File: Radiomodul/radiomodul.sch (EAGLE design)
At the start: 39 parts, among them IC1 ATMEGA2561-16AI, IC2 MCP42050, IC3 E910.15, IC4 AVR-JTAG, IC5 MAX232ECWE, IC6 MCP601SN, IC7 TLE42754D, J1 39-30-1100, Q1 16000000

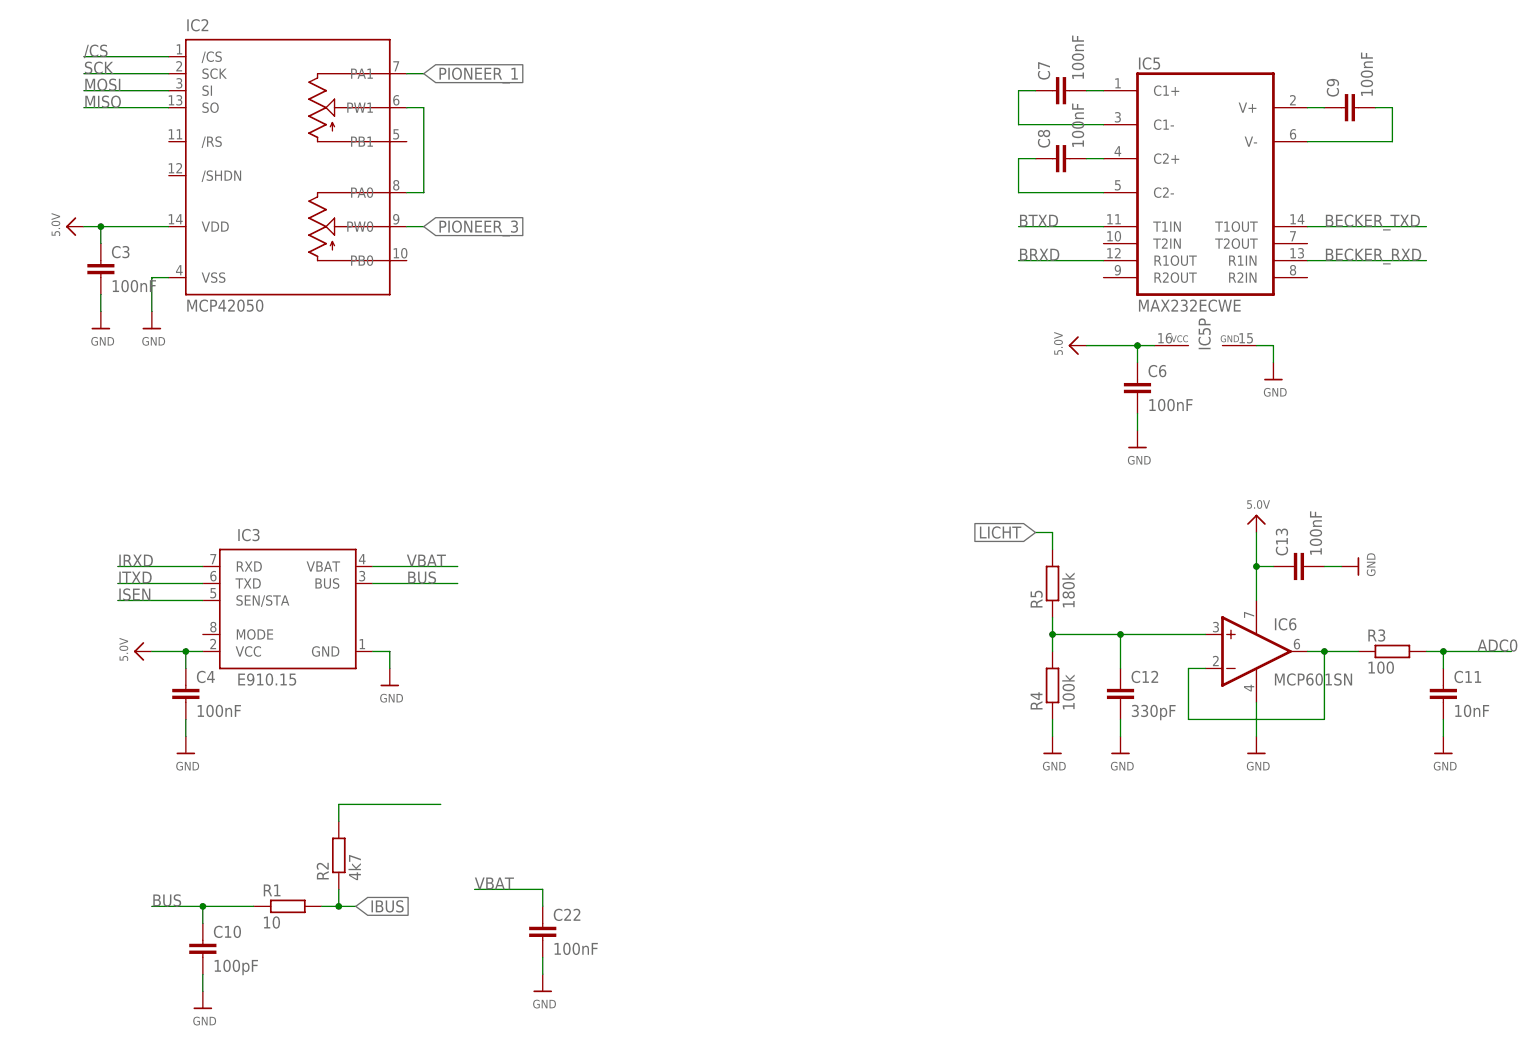
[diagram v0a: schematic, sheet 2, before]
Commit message: board and schematic replaced
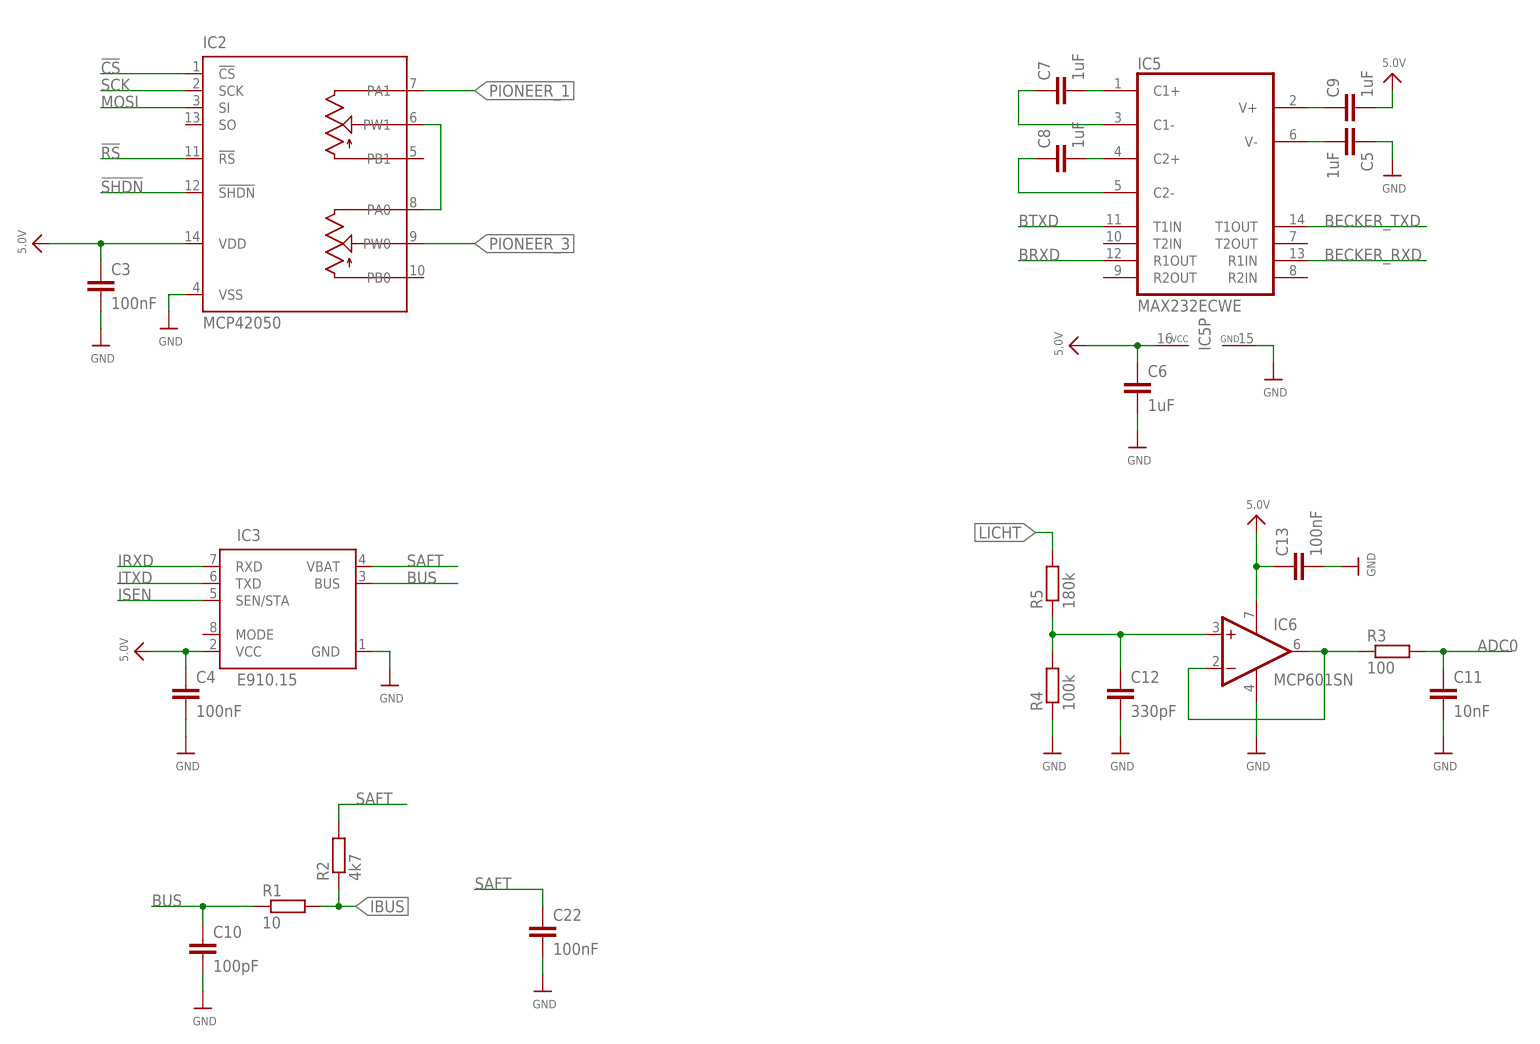
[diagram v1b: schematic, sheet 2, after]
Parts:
- added C5: 1uF, rcl:C-EUC0805
- C18, C19: value 18pF -> 22pF
- C6, C7, C8, C9: value 100nF -> 1uF
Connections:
- removed net /CS: IC1.(SS/PCINT0)PB0, IC2./CS
- removed net /RESET: IC1.RESET, IC4./RESET, IC7.RO, R6.1
- removed net MISO: IC1.(MISO/PCINT3)PB3, IC2.SO
- removed net N$9 (its old number): C9.2, IC5G$1.V-
- removed net VBAT: C22.1, IC3.VBAT
- new net !CS: IC1.(SS/PCINT0)PB0, IC2.!CS
- new net !RESET: IC1.RESET, IC4.!RESET, IC7.RO, R6.1
- new net !RS: IC1.(OC1B/PCINT6)PB6, IC2.!RS
- new net !SHDN: IC1.(OC1A/PCINT5)PB5, IC2.!SHDN
- new net N$3: C5.2, IC5G$1.V-
- net 5.0V: now also C9.2
- net GND: now also C5.1
- net SAFT: now also C22.1, IC3.VBAT
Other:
- moved on the sheet: C3, D1, IC2, R6
